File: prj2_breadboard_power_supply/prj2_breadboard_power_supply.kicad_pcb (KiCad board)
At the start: 2 copper layers, 35.6 x 52.7 mm, 17 parts, among them J1 Conn_01x02_Pin, J2 Conn_01x02_Pin, J3 Conn_01x03_Pin, J4 Conn_01x03_Pin, J5 Screw_Terminal_01x02, J6 Barrel_Jack_Switch, J7 Screw_Terminal_01x02, U1 LM7805_TO220, U2 LM317_TO-220

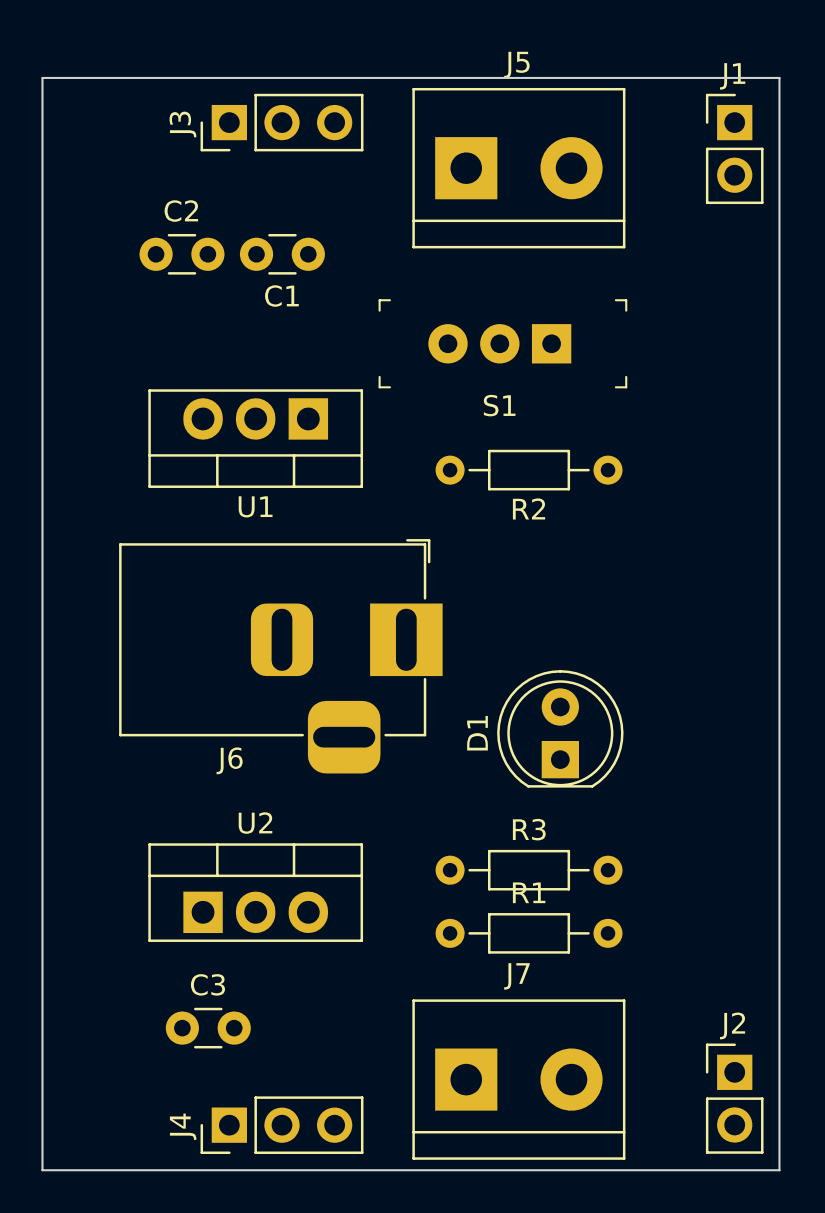
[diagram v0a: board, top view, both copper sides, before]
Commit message: Conclusione design PCB progetto 2
Feat: create tutte le connessioni tra i componenti
Feat: aggiustata la silkscreen
Fix: modificato il posizionamento di alcuni componenti
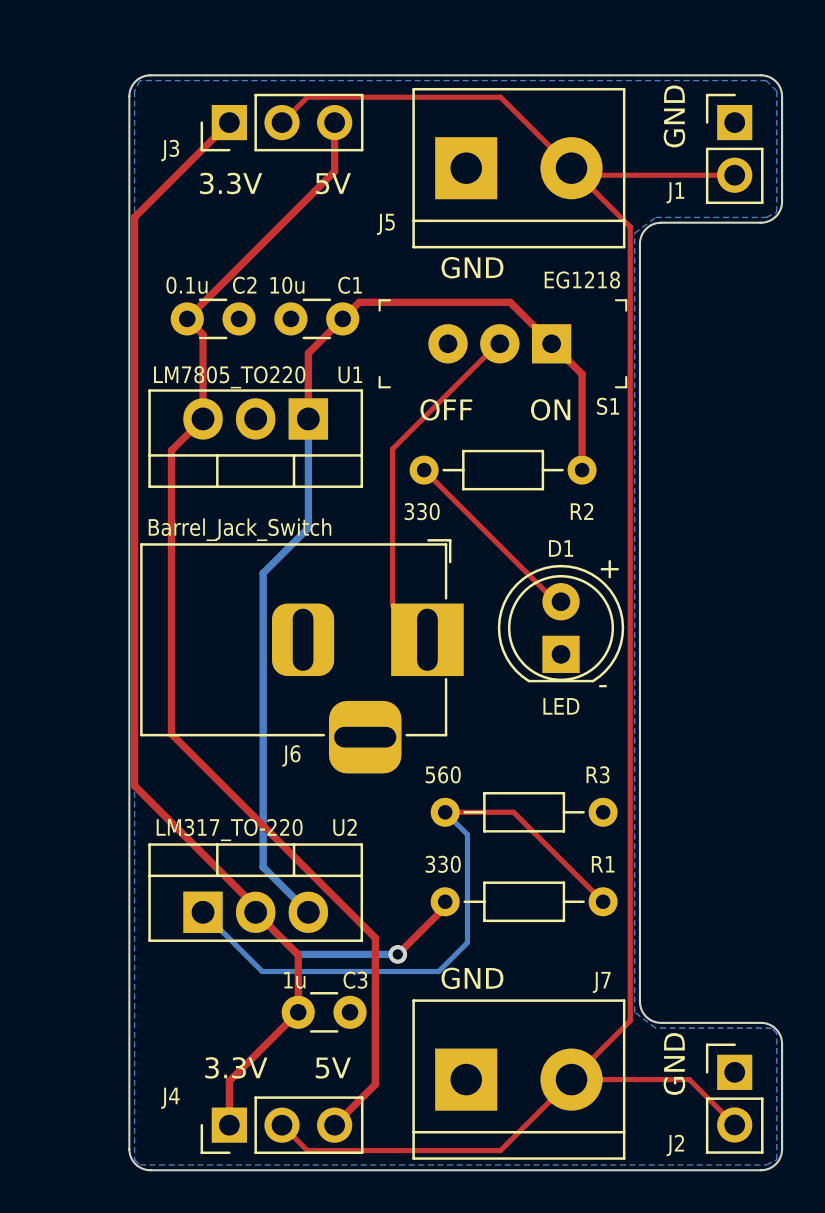
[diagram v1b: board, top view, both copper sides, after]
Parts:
- added REF**: OSHW-Logo_5.7x6mm_SilkScreen, Symbol:OSHW-Logo_5.7x6mm_SilkScreen, B.Cu at (94.0, 91.4)
- added REF**: KiCad-Logo2_5mm_SilkScreen, Symbol:KiCad-Logo2_5mm_SilkScreen, B.Cu at (109.2, 96.5)
- moved C3 5.64 mm to (98.3, 103.9)
- moved D1 5.08 mm to (111.0, 86.6)
- moved C1 3.53 mm to (100.5, 70.4)
- moved C2 3.46 mm to (93.0, 70.4)
- moved R3 2.80 mm to (105.4, 94.2)
- moved R1 1.54 mm to (105.4, 98.6)
- moved R2 1.25 mm to (112.0, 77.7)
- moved J6 1.02 mm to (104.6, 85.9)
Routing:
- net /PWR_output: track 0.00 -> 94.9 mm
- net /3.3V: track 0.00 -> 66.2 mm, vias 0 -> 1
- net /5V: track 0.00 -> 57.2 mm
- net /12V: track 0.00 -> 49.1 mm
- net Net-(U2-ADJ): track 0.00 -> 30.7 mm
- net /PWR_input: track 0.00 -> 17.2 mm
- net Net-(D1-A): track 0.00 -> 9.23 mm
- added copper zone on B.Cu, net GND
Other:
- board size 35.6 x 52.7 mm -> 31.5 x 52.8 mm
- board text added: "+"
- board text added: "-"
- board text added: "3.3V"
- board text added: "5V"
- board text added: "Breadboard Power Supply"
- board text added: "GND"
- board text added: "OFF"
- board text added: "ON"
- board text added: "v0.1"

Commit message: Correzione schematico e PCB progetto 2
Fix: rimosso corto circuito tra pin 2 di J3 e J4
Feat: aggiornati i settaggi della pagina nel PCB
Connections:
- J1 pad 2: /PWR_output -> /PWR_OUT_TOP
- J2 pad 2: /PWR_output -> /PWR_OUT_BOTTOM
- J3 pad 2: /PWR_output -> /PWR_OUT_TOP
- J4 pad 2: /PWR_output -> /PWR_OUT_BOTTOM
- J5 pad 2: /PWR_output -> /PWR_OUT_TOP
- J7 pad 2: /PWR_output -> /PWR_OUT_BOTTOM
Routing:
- net /PWR_output: track 94.9 -> 0.00 mm
- net /PWR_OUT_BOTTOM: track 0.00 -> 24.7 mm
- net /PWR_OUT_TOP: track 0.00 -> 24.0 mm
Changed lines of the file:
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@@
   )
   (paper "A4")
+  (title_block
+    (title "Learning KiCad with a simple project")
+    (date "2023-06-21")
+    (rev "2")
+    (company "Filippo Graziani")
+  )
   (layers
     (0 "F.Cu" signal)
@@
   (net 4 "/3.3V")
   (net 5 "Net-(D1-A)")
-  (net 6 "/PWR_output")
+  (net 6 "/PWR_OUT_TOP")
   (net 7 "/PWR_input")
   (net 8 "Net-(U2-ADJ)")
   (net 9 "unconnected-(S1-Pad3)")
+  (net 10 "/PWR_OUT_BOTTOM")
   (footprint "Resistor_THT:R_Axial_DIN0204_L3.6mm_D1.6mm_P7.62mm_Horizontal" (layer "F.Cu")
     (at 105.41 94.234)
@@
       (net 2 "GND") (pinfunction "Pin_1") (pintype "passive"))
     (pad "2" thru_hole circle locked (at 5.08 0) (size 3 3) (drill 1.52) (layers "*.Cu" "*.Mask")
-      (net 6 "/PWR_output") (pinfunction "Pin_2") (pintype "passive"))
+      (net 6 "/PWR_OUT_TOP") (pinfunction "Pin_2") (pintype "passive"))
     (model "${KICAD6_3DMODEL_DIR}/TerminalBlock.3dshapes/TerminalBlock_bornier-2_P5.08mm.wrl"
       (offset (xyz 2.539999962 0 0))
@@
       (net 2 "GND") (pinfunction "Pin_1") (pintype "passive"))
     (pad "2" thru_hole oval locked (at 0 2.54) (size 1.7 1.7) (drill 1) (layers "*.Cu" "*.Mask")
-      (net 6 "/PWR_output") (pinfunction "Pin_2") (pintype "passive"))
+      (net 6 "/PWR_OUT_TOP") (pinfunction "Pin_2") (pintype "passive"))
     (model "${KICAD6_3DMODEL_DIR}/Connector_PinHeader_2.54mm.3dshapes/PinHeader_1x02_P2.54mm_Vertical.wrl"
       (offset (xyz 0 0 0))
@@
       (net 4 "/3.3V") (pinfunction "Pin_1") (pintype "passive"))
     (pad "2" thru_hole oval locked (at 0 2.54 90) (size 1.7 1.7) (drill 1) (layers "*.Cu" "*.Mask")
-      (net 6 "/PWR_output") (pinfunction "Pin_2") (pintype "passive"))
+      (net 6 "/PWR_OUT_TOP") (pinfunction "Pin_2") (pintype "passive"))
     (pad "3" thru_hole oval locked (at 0 5.08 90) (size 1.7 1.7) (drill 1) (layers "*.Cu" "*.Mask")
       (net 3 "/5V") (pinfunction "Pin_3") (pintype "passive"))
@@
       (net 2 "GND") (pinfunction "Pin_1") (pintype "passive"))
     (pad "2" thru_hole circle locked (at 5.08 0) (size 3 3) (drill 1.52) (layers "*.Cu" "*.Mask")
-      (net 6 "/PWR_output") (pinfunction "Pin_2") (pintype "passive"))
+      (net 10 "/PWR_OUT_BOTTOM") (pinfunction "Pin_2") (pintype "passive"))
     (model "${KICAD6_3DMODEL_DIR}/TerminalBlock.3dshapes/TerminalBlock_bornier-2_P5.08mm.wrl"
       (offset (xyz 2.539999962 0 0))
@@
       (net 2 "GND") (pinfunction "Pin_1") (pintype "passive"))
     (pad "2" thru_hole oval locked (at 0 2.54) (size 1.7 1.7) (drill 1) (layers "*.Cu" "*.Mask")
-      (net 6 "/PWR_output") (pinfunction "Pin_2") (pintype "passive"))
+      (net 10 "/PWR_OUT_BOTTOM") (pinfunction "Pin_2") (pintype "passive"))
     (model "${KICAD6_3DMODEL_DIR}/Connector_PinHeader_2.54mm.3dshapes/PinHeader_1x02_P2.54mm_Vertical.wrl"
       (offset (xyz 0 0 0))
@@
       (net 4 "/3.3V") (pinfunction "Pin_1") (pintype "passive"))
     (pad "2" thru_hole oval locked (at 0 2.54 90) (size 1.7 1.7) (drill 1) (layers "*.Cu" "*.Mask")
-      (net 6 "/PWR_output") (pinfunction "Pin_2") (pintype "passive"))
+      (net 10 "/PWR_OUT_BOTTOM") (pinfunction "Pin_2") (pintype "passive"))
     (pad "3" thru_hole oval locked (at 0 5.08 90) (size 1.7 1.7) (drill 1) (layers "*.Cu" "*.Mask")
       (net 3 "/5V") (pinfunction "Pin_3") (pintype "passive"))
@@
     (effects (font (size 1 1) (thickness 0.15)) (justify left bottom))
   )
-  (gr_text "GND" (at 117.094 107.95 90) (layer "F.SilkS")
-    (effects (font (size 1 1) (thickness 0.15)) (justify left bottom))
-  )
   (gr_text "GND" (at 105.156 102.87) (layer "F.SilkS")
     (effects (font (size 1 1) (thickness 0.15)) (justify left bottom))
@@
   (segment (start 104.394 77.724) (end 110.744 84.074) (width 0.25) (layer "F.Cu") (net 5))
   (segment (start 110.744 84.074) (end 110.998 84.074) (width 0.25) (layer "F.Cu") (net 5))
-  (segment (start 114.341 104.2966) (end 114.341 65.99) (width 0.25) (layer "F.Cu") (net 6))
-  (segment (start 97.536 109.3316) (end 98.761 110.5566) (width 0.25) (layer "F.Cu") (net 6))
-  (segment (start 111.506 107.1316) (end 114.341 104.2966) (width 0.25) (layer "F.Cu") (net 6))
-  (segment (start 117.19 107.1316) (end 119.38 109.3216) (width 0.25) (layer "F.Cu") (net 6))
-  (segment (start 114.341 65.99) (end 111.506 63.155) (width 0.25) (layer "F.Cu") (net 6))
-  (segment (start 111.506 107.1316) (end 117.19 107.1316) (width 0.25) (layer "F.Cu") (net 6))
-  (segment (start 97.536 60.955) (end 98.761 59.73) (width 0.25) (layer "F.Cu") (net 6))
-  (segment (start 108.081 59.73) (end 111.506 63.155) (width 0.25) (layer "F.Cu") (net 6))
-  (segment (start 98.761 110.5566) (end 108.081 110.5566) (width 0.25) (layer "F.Cu") (net 6))
-  (segment (start 108.081 110.5566) (end 111.506 107.1316) (width 0.25) (layer "F.Cu") (net 6))
-  (segment (start 98.761 59.73) (end 108.081 59.73) (width 0.25) (layer "F.Cu") (net 6))
-  (segment (start 111.846 63.495) (end 111.506 63.155) (width 0.25) (layer "F.Cu") (net 6))
-  (segment (start 119.38 63.495) (end 111.846 63.495) (width 0.25) (layer "F.Cu") (net 6))
+  (segment (start 98.811 59.68) (end 108.031 59.68) (width 0.35) (layer "F.Cu") (net 6))
+  (segment (start 111.846 63.495) (end 111.506 63.155) (width 0.35) (layer "F.Cu") (net 6))
+  (segment (start 97.536 60.955) (end 98.811 59.68) (width 0.35) (layer "F.Cu") (net 6))
+  (segment (start 119.38 63.495) (end 111.846 63.495) (width 0.35) (layer "F.Cu") (net 6))
+  (segment (start 108.031 59.68) (end 111.506 63.155) (width 0.35) (layer "F.Cu") (net 6))
   (segment (start 102.87 76.708) (end 107.95 71.628) (width 0.25) (layer "F.Cu") (net 7))
   (segment (start 107.95 71.628) (end 108.046 71.628) (width 0.25) (layer "F.Cu") (net 7))
@@
   (segment (start 105.093 101.917) (end 96.583 101.917) (width 0.25) (layer "B.Cu") (net 8))
   (segment (start 96.583 101.917) (end 93.726 99.06) (width 0.25) (layer "B.Cu") (net 8))
+  (segment (start 119.38 109.3216) (end 113.696 109.3216) (width 0.35) (layer "F.Cu") (net 10))
+  (segment (start 98.811 110.6066) (end 108.031 110.6066) (width 0.35) (layer "F.Cu") (net 10))
+  (segment (start 97.536 109.3316) (end 98.811 110.6066) (width 0.35) (layer "F.Cu") (net 10))
+  (segment (start 108.031 110.6066) (end 111.506 107.1316) (width 0.35) (layer "F.Cu") (net 10))
+  (segment (start 113.696 109.3216) (end 111.506 107.1316) (width 0.35) (layer "F.Cu") (net 10))
   (zone (net 2) (net_name "GND") (layer "B.Cu") (hatch edge 0.5)
     (connect_pads (clearance 0.5))
